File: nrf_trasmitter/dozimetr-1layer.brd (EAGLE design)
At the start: 16 x 21.6 mm, 13 parts

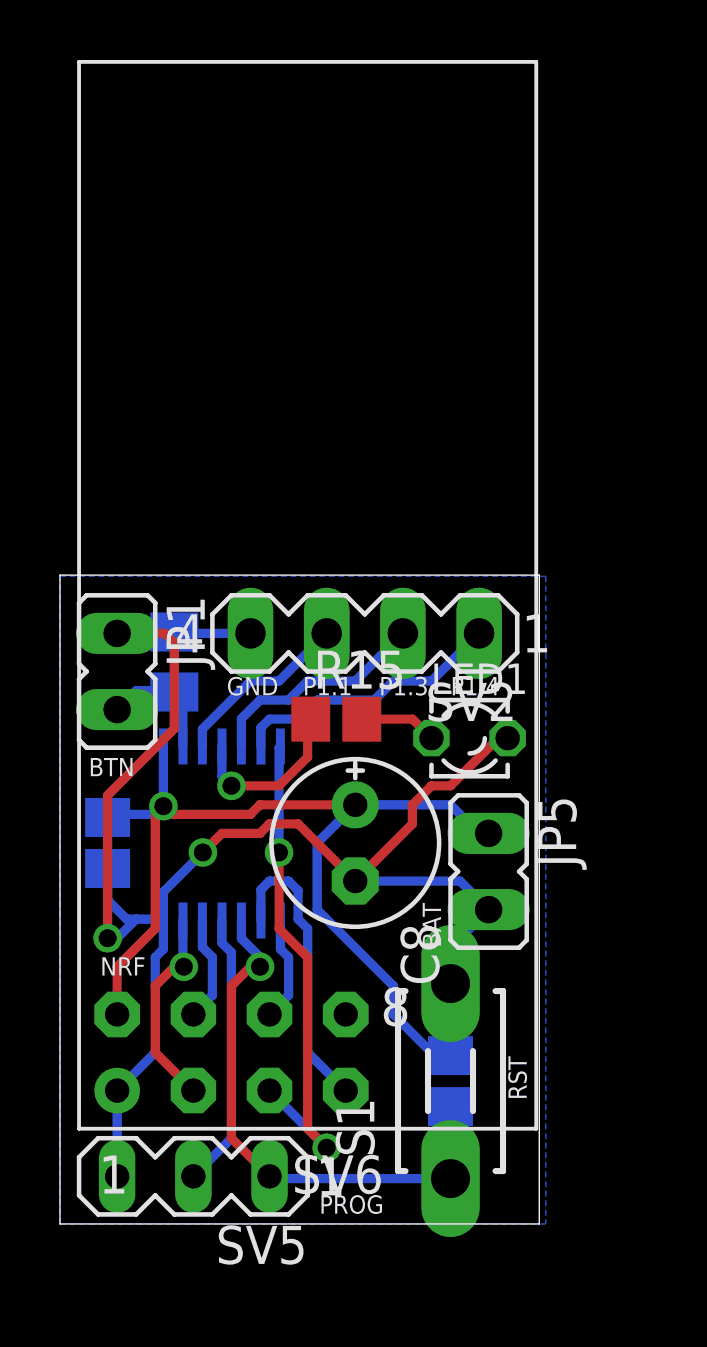
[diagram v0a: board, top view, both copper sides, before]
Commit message: Updated nrf transmitter.
BUG: exchanged MISO and MOSI on MCU!
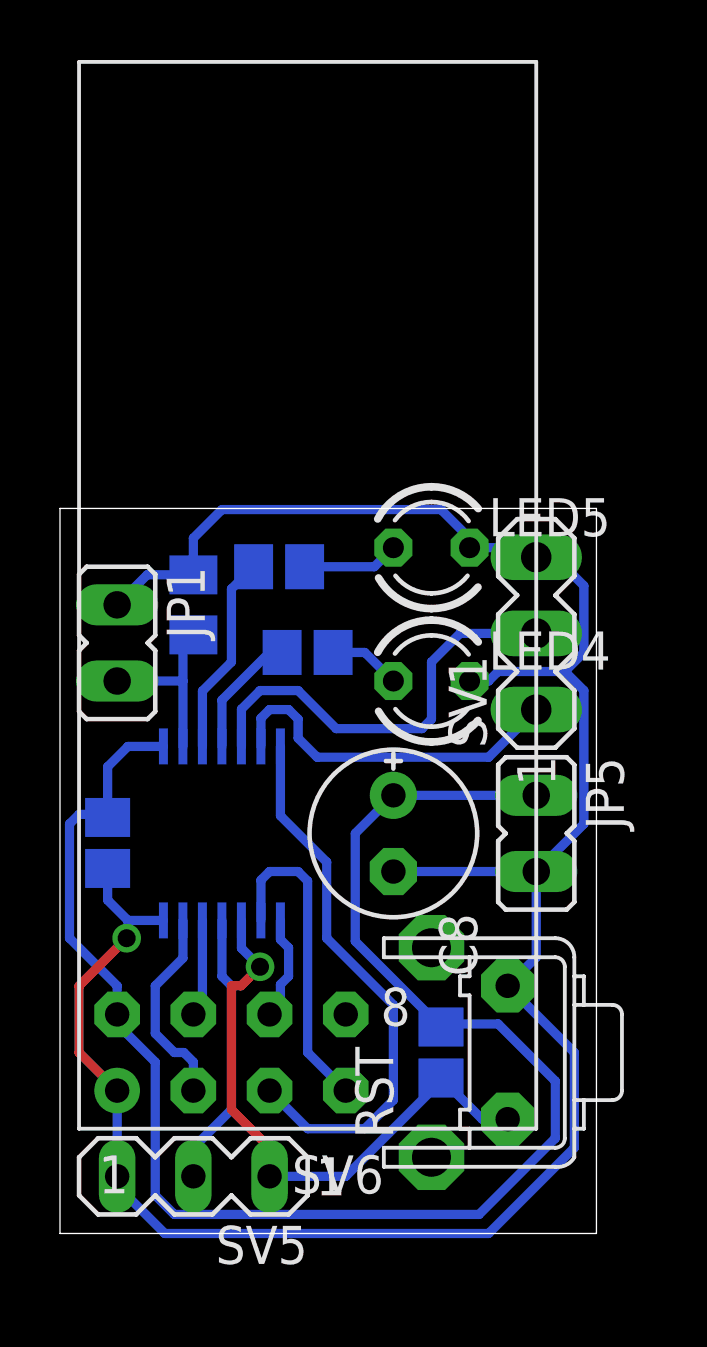
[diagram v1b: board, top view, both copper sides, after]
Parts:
- removed LED1: (no value), led:LZR181
- removed S1: DTS-3, switch-tact:DTS-3
- removed SV2: (no value), con-lstb:MA04-1
- added LED4, LED5: LED3MM, #Krakonos:LED3MM
- added R16: 330R, resistor:R0805
- added RST: P-KSM632B, #Krakonos:P-KSM632B
- added SV1: GPIO, con-lstb:MA03-1
- moved R15 2.42 mm to (12.7, 67.9), flipped to the bottom, turned to 180 degrees
- moved JP5 2.03 mm to (20.3, 61.9)
- moved C9 2.01 mm to (8.89, 69.5)
- moved C8 1.31 mm to (15.6, 61.9)
- moved R14 1.00 mm to (17.1, 54.6)
- moved JP1 0.95 mm to (6.35, 68.3)
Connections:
- removed net N$4: SV2.3, U$3.3
- new net N$50: R16.1, U$3.3
- new net N$51: LED5.A, R16.2
- net GND: now also LED4.K, LED5.K, RST.2, SV1.3; no longer LED1.K, S1.2, SV2.4
- net N$2: now also SV1.2; no longer SV2.2
- net N$3: now also SV1.1; no longer SV2.1
- net N$40: now also RST.1; no longer S1.1
- net N$47: now also LED4.A; no longer LED1.A
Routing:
- net GND: track 55.2 -> 78.5 mm, vias 2 -> 1
- net VCC: track 34.1 -> 54.3 mm, vias 1 -> 0
- net N$2: track 7.48 -> 14.3 mm
- net N$50: track 0.00 -> 6.70 mm
- net N$4: track 6.04 -> 0.00 mm
- net N$51: track 0.00 -> 3.22 mm
- net N$3: track 9.20 -> 11.9 mm
- net N$1: track 4.26 -> 6.06 mm
- net N$43: track 16.7 -> 18.4 mm, vias 2 -> 0
- net N$46: track 5.69 -> 4.21 mm, vias 1 -> 0
- net N$40: track 18.4 -> 19.8 mm
- net N$41: track 9.84 -> 10.7 mm
- net N$48: track 6.79 -> 6.77 mm, vias 1 -> 0
- removed copper zone on layer 16, net GND
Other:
- board size 16 x 21.6 mm -> 17.9 x 24.2 mm
- board text removed: "+"
- board text removed: "-"
- board text removed: "BAT"
- board text removed: "BTN"
- board text removed: "GND"
- board text removed: "Jethro"
- board text removed: "MSP430-NRF"
- board text removed: "NRF"
- board text removed: "P1.0"
- board text removed: "P1.1"
- board text removed: "P1.3"
- board text removed: "P1.4"
- board text removed: "PROG"
- board text removed: "RST"
- board text removed: "TST"
